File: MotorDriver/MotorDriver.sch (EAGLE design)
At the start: 89 parts, among them IC1 DRV8320RSRHAR, IC2 MAX3051ESA+, IC3 TPD4S014DSQR, J1 J_USB_MICROAB_HIROSE_ZX62-AB-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, J2 SM03B-ZESS-TB, Q1 BUK7Y7R8-80EX, Q2 BUK7Y7R8-80EX, Q3 BUK7Y7R8-80EX, Q4 BUK7Y7R8-80EX, Q5 BUK7Y7R8-80EX, Q6 BUK7Y7R8-80EX, U1 LPC1549JBD48, U2 ADCMP350YKSZ, U3 MCP1700T-33, U4 ADR5041, U5 AS5145B, Y1 FA238V

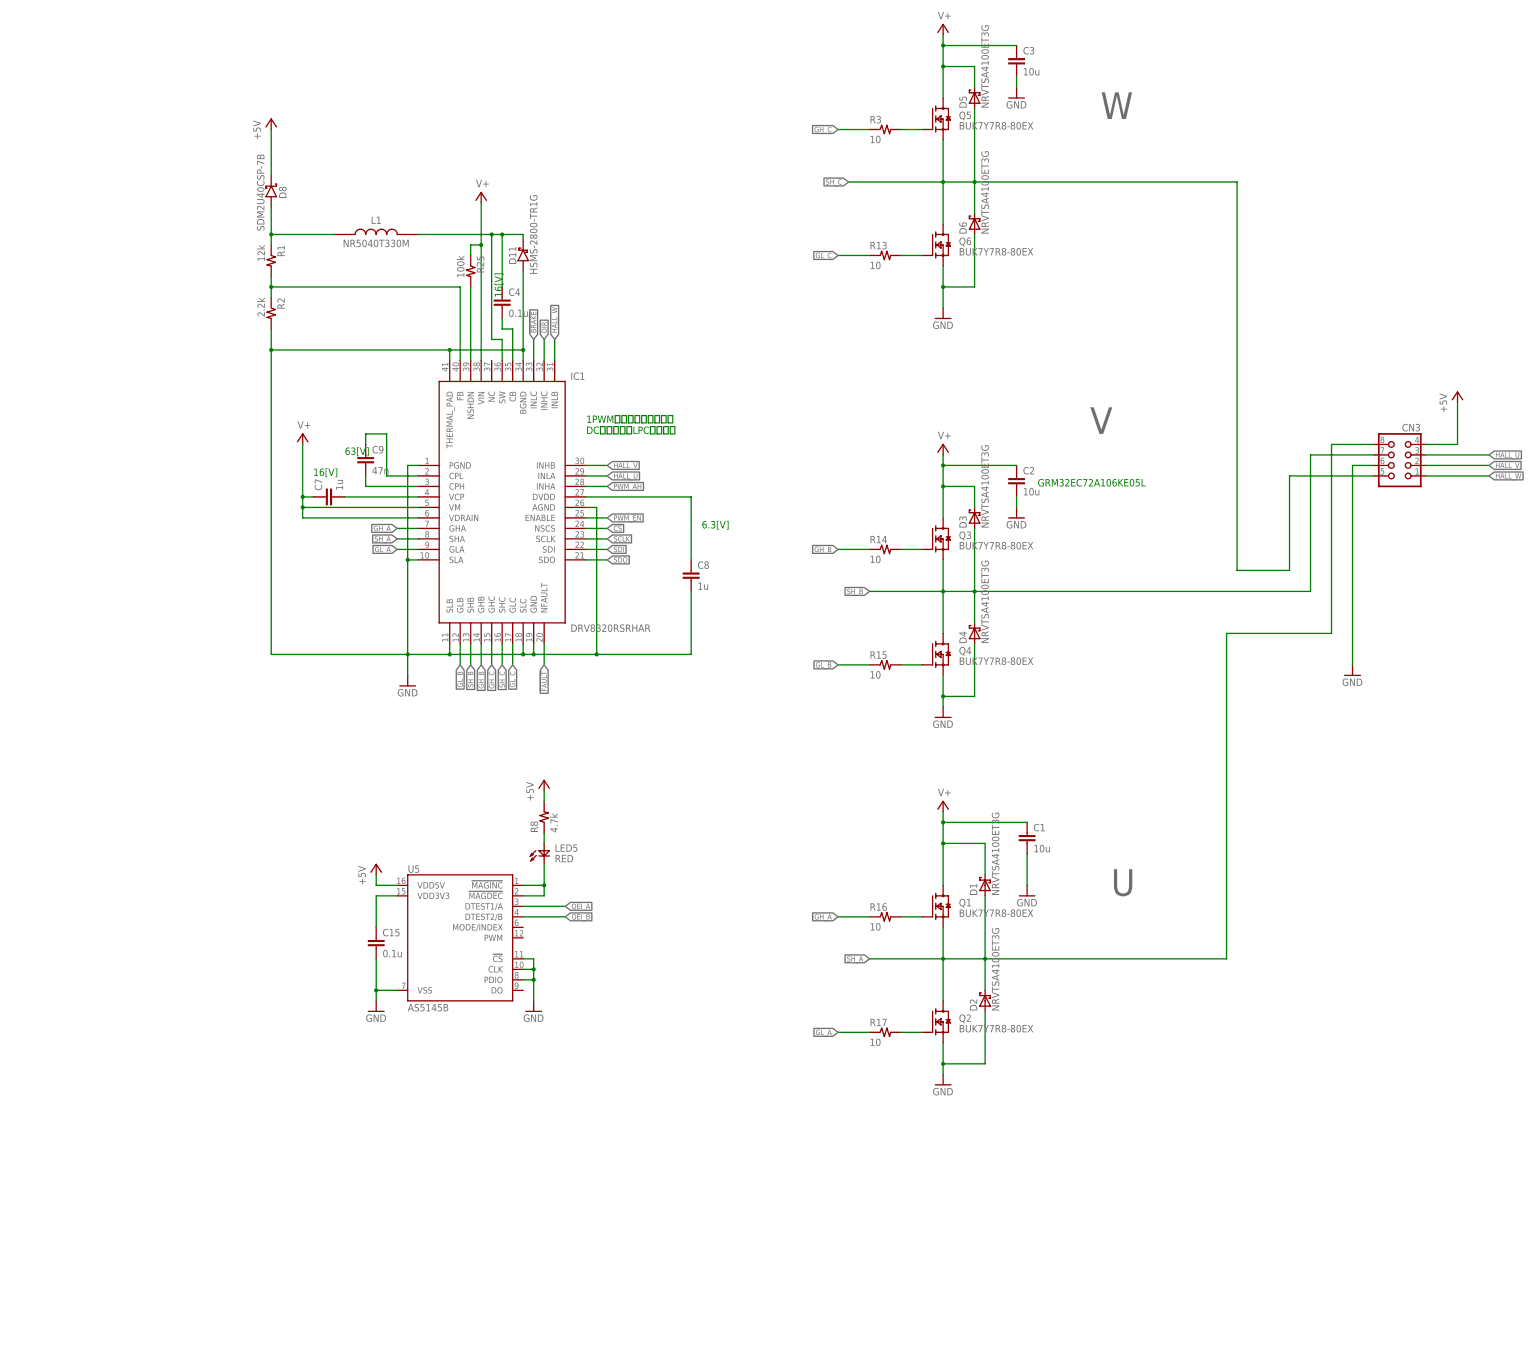
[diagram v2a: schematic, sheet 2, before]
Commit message: [fix]仕様確定に伴って変更
*電源電圧を24[V]に
*エンコーダICが廃盤になったので変更
*電源強化
*部品票の更新
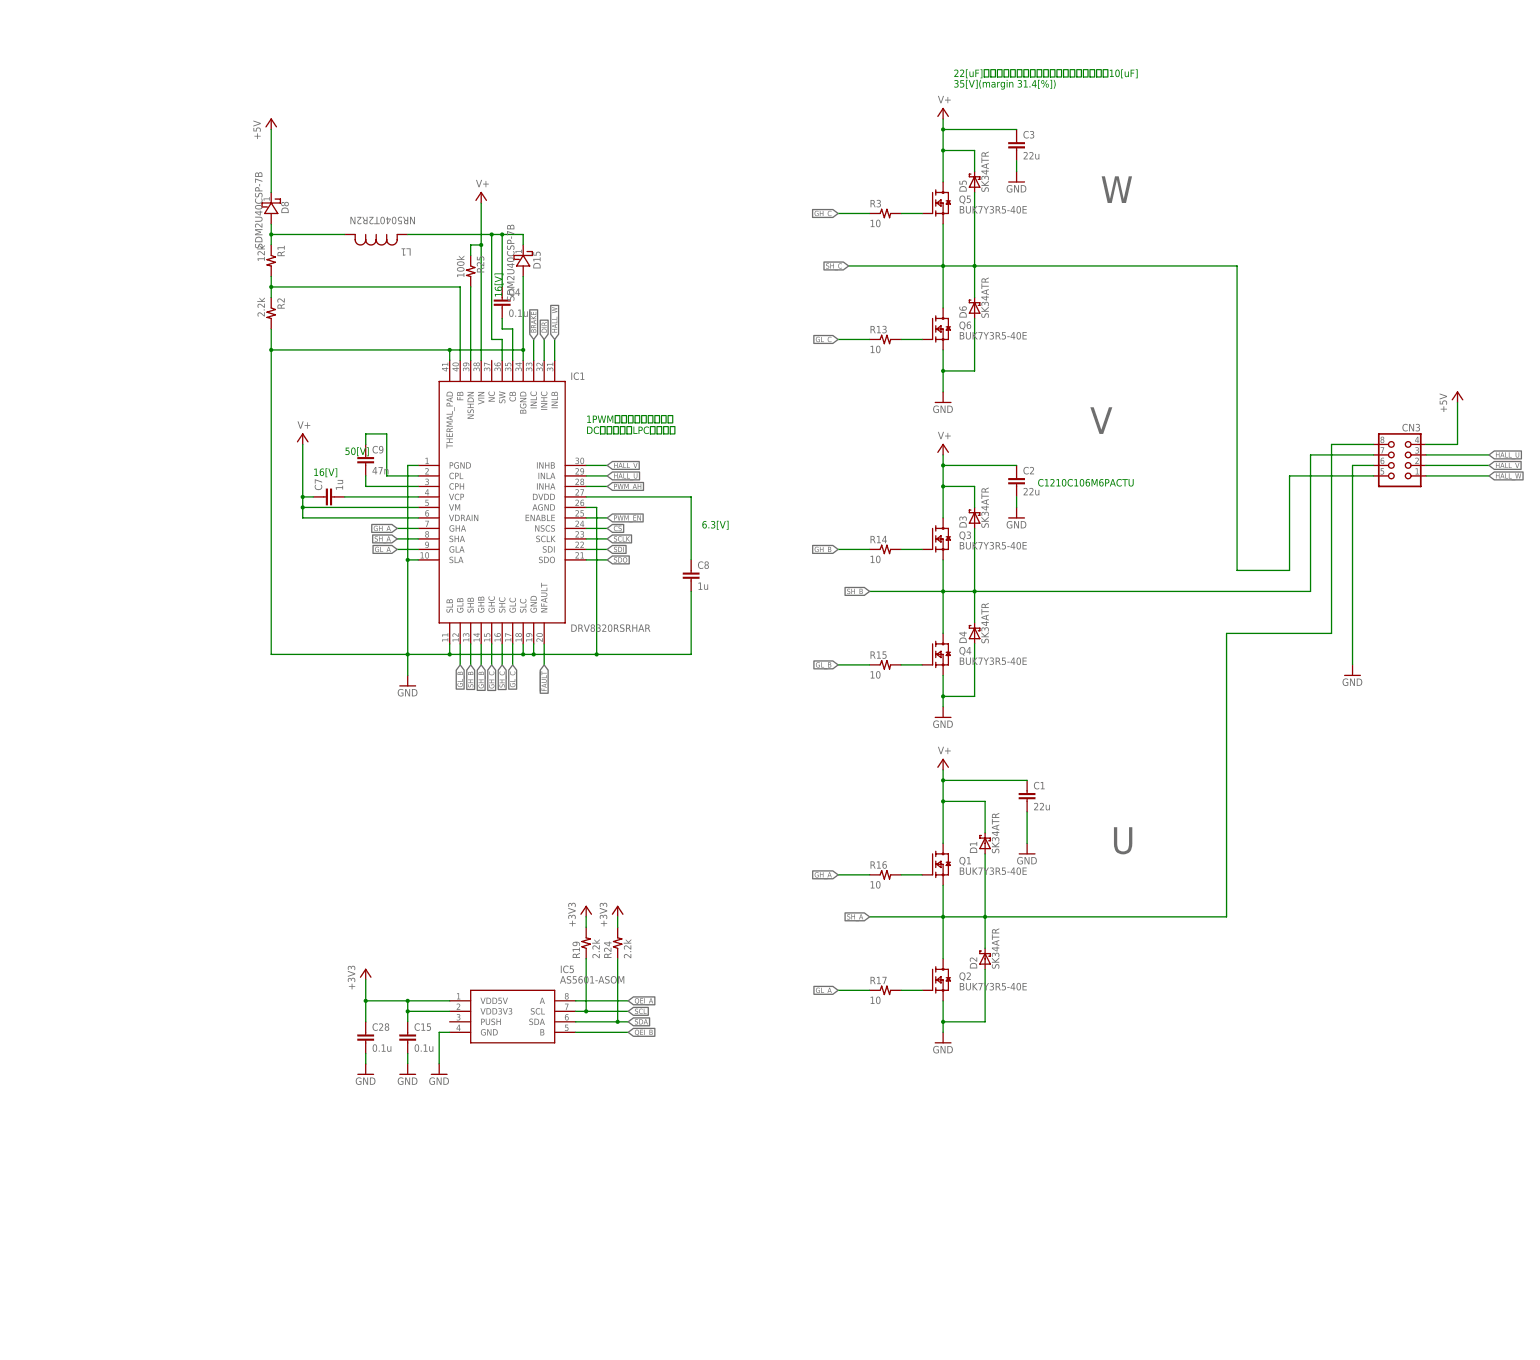
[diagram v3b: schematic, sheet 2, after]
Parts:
- removed D11: HSMS-2800-TR1G, HSMS-2800-TR1G:HSMS-2800-TR1G
- removed LED5: RED, MotorDriver:LED1608
- removed R8: 4.7k, MotorDriver:R1005
- removed U5: AS5145B, ic-ams:AS5145B
- added C17, C18, C21, C25, C26, C27: 10u, MotorDriver:C3225
- added C28: 0.1u, MotorDriver:C1005
- added D15: SDM2U40CSP-7B, SDM2U40CSP-7B:SDM2U40CSP-7B
- added IC5: AS5601-ASOM, AS5601-ASOM:AS5601-ASOM
- added R19, R24: 2.2k, MotorDriver:R1005
- C1, C2, C3: value 10u -> 22u
- C13, C16: value 22u -> 10u; device Passive:CPOLS-6.3 -> MotorDriver:C3225
- C14, C5: value 0.47u -> 47n
- C4, C9: device MotorDriver:C1608 -> MotorDriver:C1005
- CN3: device con-Molex:43045-0800 -> MotorDriver:43045-0800
- D1, D2, D3, D4, D5, D6: value NRVTSA4100ET3G -> SK34ATR
- D10: value SMAJ54A -> SMAJP4KE30A
- D13: device Diode:DIODE-SMPC -> diode:DIODE-SMPC
- D7: value SDM2U40CSP-7B -> (none); device SDM2U40CSP-7B:SDM2U40CSP-7B -> MotorDriver:SBD-SOD523
- L1: value NR5040T330M -> NR5040T2R2N; device NR5040T330M:NR5040T330M -> nr5040:NR5040T2R2N
- LED4: value (none) -> RED
- Q1, Q2, Q3, Q4, Q5, Q6: value BUK7Y7R8-80EX -> BUK7Y3R5-40E; device MotorDriver:BUK7Y7R8-80EX -> NXP_60_26022015:BUK7Y3R5-40E
- R10, R22, R9: device MotorDriver:R1608 -> MotorDriver:R1005
- R20: value 47k -> 22k; device MotorDriver:R1608 -> MotorDriver:R1005
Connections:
- removed net N$29: C15.1, U5.VDD3V3
- removed net N$30: LED5.K, U5.!MAGDEC, U5.!MAGINC
- removed net N$32: LED5.A, R8.1
- new net SCL: IC5.SCL, R19.1, U1.PIO0_22/I2C0_SCL
- new net SDA: IC5.SDA, R24.1, U1.PIO0_23/I2C0_SDA
- net +3V3: now also C15.1, C28.1, IC5.VDD3V3, IC5.VDD5V, R19.2, R24.2
- net +5V: no longer R8.2, U5.VDD5V
- net GND: now also C13.2, C16.2, C17.2, C18.2, C21.2, C25.2, C26.2, C27.2, C28.2, D15.A, IC5.GND; no longer C13.N, C16.N, D11.ANODE, U5.!CS, U5.CLK, U5.PDIO, U5.VSS
- net N$3: now also D15.K; no longer D11.CATHODE
- net QEI_A: now also IC5.A; no longer U5.DTEST1/A
- net QEI_B: now also IC5.B; no longer U5.DTEST2/B
- net V+: now also C13.1, C16.1, C17.1, C18.1, C21.1, C25.1, C26.1, C27.1; no longer C13.P, C16.P
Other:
- note added: "14～24[V] 9.6[V]以下はヒューズ切断と誤検知"
- note added: "22[uF]が欲しいけど在庫切れが著しいので暫定で10[uF]"
- note added: "35[V](margin 31.4[%])"
- note added: "50[V]"
- note added: "C1210C106M6PACTU"
- note added: "V-= 0.6[V]@V+=9.6[V] 1.0[V]@V+=16[V] 1.5[V]@V+=24[V]"
- note added: "VBAT= 1.09[V]@V+=12[V] 1.45[V]@V+=16[V] 2.18[V]@V+=24[V]"
- note removed: "14～50[V] 9.6[V]以下はヒューズ切断と誤検知"
- note removed: "63[V]"
- note removed: "GRM32EC72A106KE05L"
- note removed: "V-= 0.6[V]@V+=9.6[V] 1.0[V]@V+=16[V] 1.5[V]@V+=24[V] 3.2[V]@V+=52[V]"
- note removed: "VBAT= 0.537[V]@V+=12[V] 0.715[V]@V+=16[V] 1.073[V]@V+=24[V] 2.146[V]@V+=48[V]"
- moved on the sheet: C1, C15, C3, D1, D10, D2, D5, D6, R13, R16, R17, R3

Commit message: tmpからもってきた
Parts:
- removed D14: RB520S, MotorDriver:SBD-SOD523
- removed D15: SDM2U40CSP-7B, SDM2U40CSP-7B:SDM2U40CSP-7B
- removed IC1: DRV8320RSRHAR, DRV8320RSRHAR:DRV8320RSRHAR
- removed LED4: RED, MotorDriver:LED1608
- removed R10: 2.2k, MotorDriver:R1005
- removed R11: 330, MotorDriver:R1005
- removed R9: 33k, MotorDriver:R1005
- removed U2: ADCMP350YKSZ, adcmp350:ADCMP350YKSZ
- added C29, C31: 1u, MotorDriver:C1005
- added C30: 47n, MotorDriver:C1005
- added IC4: DRV8320SRTVT, DRV8320SRTVT:DRV8320SRTVT
- added IC6: LM5160QPWPRQ1, LM5160QPWPRQ1:LM5160QPWPRQ1
- added R27: 2.2k, MotorDriver:R1005
- added R28: 2.2, MotorDriver:R1005
- added R8: 51k, MotorDriver:R1005
- C14: value 47n -> 10u; device MotorDriver:C1005 -> MotorDriver:C3225
- C4: value 0.1u -> 10n
- C7: value 1u -> 0.1u
- C8: value 1u -> 4.7u; device MotorDriver:C1005 -> Passive:C1608
- C9: value 47n -> 22n
- L1: value NR5040T2R2N -> 15u; device nr5040:NR5040T2R2N -> Passive:L50
- R1: value 12k -> 120k
- R2: value 2.2k -> 10k
- R25: value 100k -> 3.3k
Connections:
- removed net FUSE: LED4.A, U1.SWDIO/PIO0_20/SCT1_OUT6/TMS, U2P.OUT
- removed net N$20: IC1.NSHDN, R25.2
- removed net N$25: C14.2, D14.A, R10.2, R9.1, U2P.-
- removed net N$27: LED4.K, R11.2
- new net N$32: C31.1, IC4.DVDD
- new net N$48: C30.1, IC4.CPL
- new net N$55: C29.2, IC4.VCP
- new net N$56: C30.2, IC4.CPH
- new net VBAT/2: CN5.P, F1.2, IC6.VIN, R1.2, R8.1
- net !BRAKE: now also IC4.INLC; no longer IC1.INLC
- net !CS: now also IC4.NSCS; no longer IC1.NSCS
- net !FAULT: now also IC4.NFAULT; no longer IC1.NFAULT
- net +3V3: no longer D14.K, U2A.VCC
- net DIR: now also IC4.INHC; no longer IC1.INHC
- net GH_A: now also IC4.GHA; no longer IC1.GHA
- net GH_B: now also IC4.GHB; no longer IC1.GHB
- net GH_C: now also IC4.GHC; no longer IC1.GHC
- net GL_A: now also IC4.GLA; no longer IC1.GLA
- net GL_B: now also IC4.GLB; no longer IC1.GLB
- net GL_C: now also IC4.GLC; no longer IC1.GLC
- net GND: now also C14.2, C31.2, C7.1, C8.1, C9.1, IC4.AGND, IC4.PGND, IC4.SLA, IC4.SLB, IC4.SLC, IC4.THERMAL_PAD, IC6.AGND, IC6.PGND, IC6.THERMAL_PAD_(AGND), R2.1, R27.2; no longer C14.1, C8.2, D15.A, IC1.AGND, IC1.BGND, IC1.GND, IC1.PGND, IC1.SLA, IC1.SLB, IC1.SLC, IC1.THERMAL_PAD, R10.1, R11.1, R2.2, U2A.GND
- net HALL_U: now also IC4.INLA; no longer IC1.INLA
- net HALL_V: now also IC4.INHB; no longer IC1.INHB
- net HALL_W: now also IC4.INLB; no longer IC1.INLB
- net N$1: now also C7.2, IC6.FPWM, IC6.VCC; no longer IC1.FB, R1.2, R2.1
- net N$16: now also C4.1, IC6.SW(1), IC6.SW(2), L1.1; no longer C7.2, IC1.VCP
- net N$17: now also IC6.FB, R25.2, R27.1; no longer C8.1, IC1.DVDD
- net N$18: now also C4.2, IC6.BST; no longer C9.1, IC1.CPL
- net N$19: now also C8.2, R28.2; no longer C9.2, IC1.CPH
- net N$2: now also IC6.RON, R8.2; no longer D8.A, L1.1, R1.1
- net N$26: now also D8.A, L1.2, R25.1, R28.1; no longer CN5.P, F1.2
- net N$3: now also IC6.EN/UVLO, R1.1, R2.2; no longer C4.1, D15.K, IC1.SW, L1.2
- net N$4: now also C9.2, IC6.SS; no longer C4.2, IC1.CB
- net PWM_AH: now also IC4.INHA; no longer IC1.INHA
- net PWM_EN: now also IC4.ENABLE; no longer IC1.ENABLE
- net SCLK: now also IC4.SCLK; no longer IC1.SCLK
- net SDI: now also IC4.SDI; no longer IC1.SDI
- net SDO: now also IC4.SDO; no longer IC1.SDO
- net SH_A: now also IC4.SHA; no longer IC1.SHA
- net SH_B: now also IC4.SHB; no longer IC1.SHB
- net SH_C: now also IC4.SHC; no longer IC1.SHC
- net V+: now also C14.1, C29.1, IC4.VDRAIN, IC4.VM; no longer C7.1, IC1.VDRAIN, IC1.VIN, IC1.VM, R25.1, R9.2
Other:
- note added: "Fsw = 980[kHz] @ Ron = 51[kohm]"
- note added: "Fsw_nominal -> 1[MHz]"
- note added: "ILpeak = 1.136[A] @ Io_max = 1.0[A]"
- note added: "Lmin = 10.2[uH]"
- note added: "deltaIL = 0.254[A] @ Vin = 19.2[V]"
- note added: "deltaIL = 0.272[A] @ Vin = 25.2[V]"
- note removed: "16[V]"
- note removed: "1PWMモードで動作させる DCモータ用にLPCとも結合"
- note removed: "50[V]"
- note removed: "6.3[V]"
- note removed: "V-= 0.6[V]@V+=9.6[V] 1.0[V]@V+=16[V] 1.5[V]@V+=24[V]"
- note removed: "ヒューズが切れていたらLEDが点灯 LPC1549にActive-Highで入力"
- moved on the sheet: C14
